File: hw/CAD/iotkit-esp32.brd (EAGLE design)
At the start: 87.3 x 72.4 mm, 14 parts, among them IC1 MCP23017SP 0x20

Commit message: Stepper an 5V
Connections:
- removed net +5V: (+)STEPPER1.1, (+)STEPPER2.1, (+)STEPPER3.1, STEPPER1.10, STEPPER2.10
- net 5V: now also (+)STEPPER1.1, (+)STEPPER2.1, (+)STEPPER3.1, STEPPER1.10, STEPPER2.10
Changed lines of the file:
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@@
 <contactref element="U$2" pad="19"/>
 <contactref element="U$1" pad="5V"/>
+<contactref element="STEPPER2" pad="10"/>
+<contactref element="(+)STEPPER3" pad="1"/>
+<contactref element="STEPPER1" pad="10"/>
+<contactref element="(+)STEPPER2" pad="1"/>
+<contactref element="(+)STEPPER1" pad="1"/>
+<wire x1="35.56" y1="68.58" x2="50.8" y2="68.58" width="0" layer="19" extent="1-1"/>
+<wire x1="20.32" y1="68.58" x2="35.56" y2="68.58" width="0" layer="19" extent="1-1"/>
+<wire x1="49.53" y1="38.1" x2="50.8" y2="68.58" width="0" layer="19" extent="1-1"/>
+<wire x1="35.56" y1="30.48" x2="49.53" y2="38.1" width="0" layer="19" extent="1-1"/>
+<wire x1="76.2" y1="38.1" x2="49.53" y2="38.1" width="0" layer="19" extent="1-1"/>
 <wire x1="5.09" y1="5.09" x2="35.56" y2="30.48" width="0" layer="19" extent="1-1"/>
 </signal>
@@
 <wire x1="5.09" y1="27.95" x2="6.91" y2="64.77" width="0" layer="19" extent="1-1"/>
 </signal>
-<signal name="+5V">
-<contactref element="STEPPER1" pad="10"/>
-<contactref element="(+)STEPPER2" pad="1"/>
-<contactref element="(+)STEPPER1" pad="1"/>
-<contactref element="STEPPER2" pad="10"/>
-<contactref element="(+)STEPPER3" pad="1"/>
-<wire x1="49.53" y1="38.1" x2="76.2" y2="38.1" width="0" layer="19" extent="1-1"/>
-<wire x1="35.56" y1="68.58" x2="49.53" y2="38.1" width="0" layer="19" extent="1-1"/>
-<wire x1="20.32" y1="68.58" x2="35.56" y2="68.58" width="0" layer="19" extent="1-1"/>
-<wire x1="50.8" y1="68.58" x2="49.53" y2="38.1" width="0" layer="19" extent="1-1"/>
-</signal>
 <signal name="PA0">

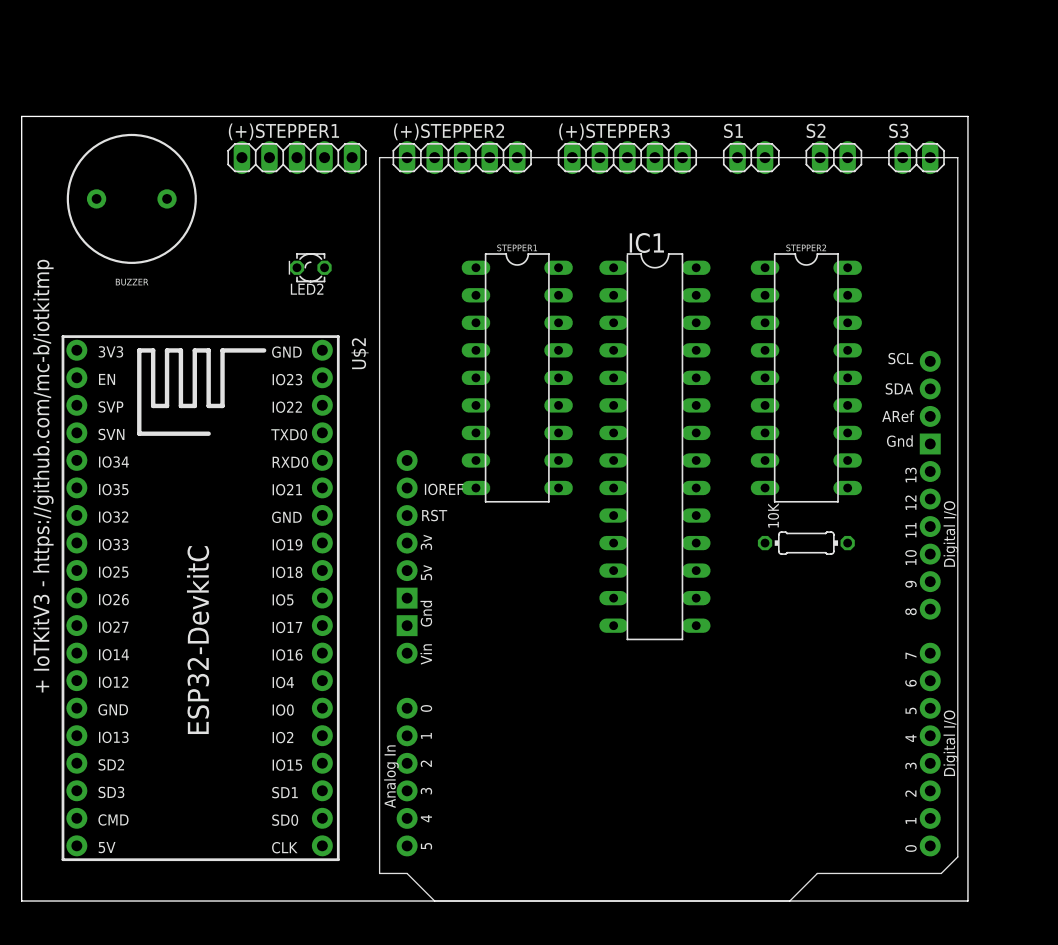
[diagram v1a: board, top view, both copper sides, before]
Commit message: Breite ESP32 falsch
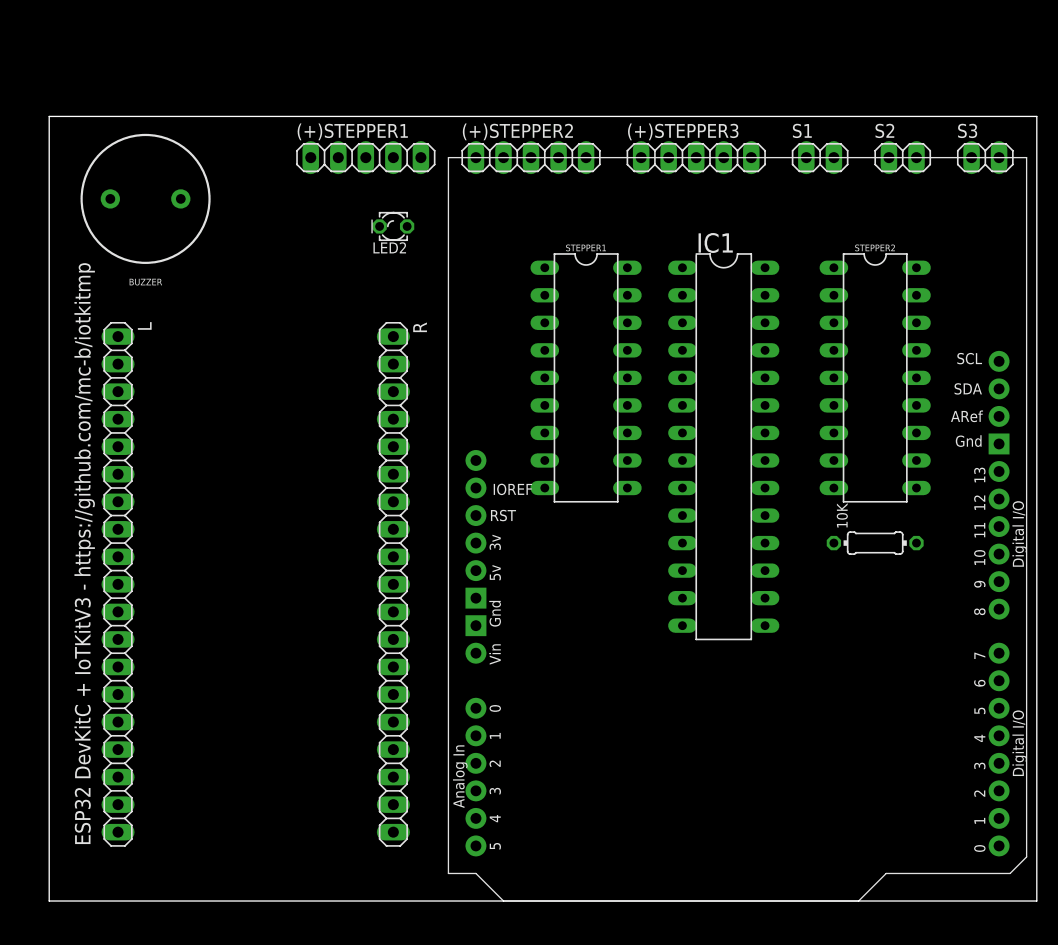
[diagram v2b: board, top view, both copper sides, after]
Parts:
- removed U$2: ESP32DEVKITC, relswitch:ESP32-DEVKITC
- added L, R: (no value), pinhead:1X19
- moved LED2 8.52 mm to (34.3, 62.2)
- moved S3 6.35 mm to (88.9, 68.6)
- moved U$1 6.35 mm to (66.0, 34.3)
- moved (+)STEPPER1 6.35 mm to (31.8, 68.6)
- moved (+)STEPPER2 6.35 mm to (47.0, 68.6)
- moved STEPPER1 6.35 mm to (52.1, 48.3)
- moved (+)STEPPER3 6.35 mm to (62.2, 68.6)
- moved 10K 6.35 mm to (78.7, 33.0)
- moved IC1 6.35 mm to (64.8, 41.9)
- moved S1 6.35 mm to (73.7, 68.6)
- moved S2 6.35 mm to (81.3, 68.6)
- moved STEPPER2 6.35 mm to (78.7, 48.3)
- moved BUZZER 1.27 mm to (11.4, 64.8)
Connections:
- net 3V3: now also L.1; no longer U$2.1
- net 5V: now also L.19; no longer U$2.19
- net A2: now also L.7; no longer U$2.7
- net A3: now also L.8; no longer U$2.8
- net A4: now also L.5; no longer U$2.5
- net A5: now also L.6; no longer U$2.6
- net BUZ: now also L.10; no longer U$2.10
- net D0: now also R.5; no longer U$2.34
- net D1: now also R.4; no longer U$2.35
- net D10: now also L.11; no longer U$2.11
- net D11: now also R.6; no longer U$2.33
- net D12: now also R.3; no longer U$2.36
- net D13: now also R.2; no longer U$2.37
- net D2: now also L.13; no longer U$2.13
- net D3: now also L.15; no longer U$2.15
- net D4: now also L.12; no longer U$2.12
- net D5: now also R.16; no longer U$2.23
- net D6: now also R.12; no longer U$2.27
- net D7: now also R.11; no longer U$2.28
- net D8: now also R.9; no longer U$2.30
- net D9: now also R.8; no longer U$2.31
- net GND: now also L.14, R.1, R.7; no longer U$2.14, U$2.32, U$2.38
- net LED1: now also R.10; no longer U$2.29
- net SCL: now also R.13; no longer U$2.26
- net SDA: now also R.15; no longer U$2.24
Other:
- board size 87.3 x 72.4 mm -> 91.1 x 72.4 mm
- board text added: "ESP32 DevKitC + IoTKitV3 - https://github.com/mc-b/iotkitmp"
- board text removed: "+ IoTKitV3 - https://github.com/mc-b/iotkitmp"

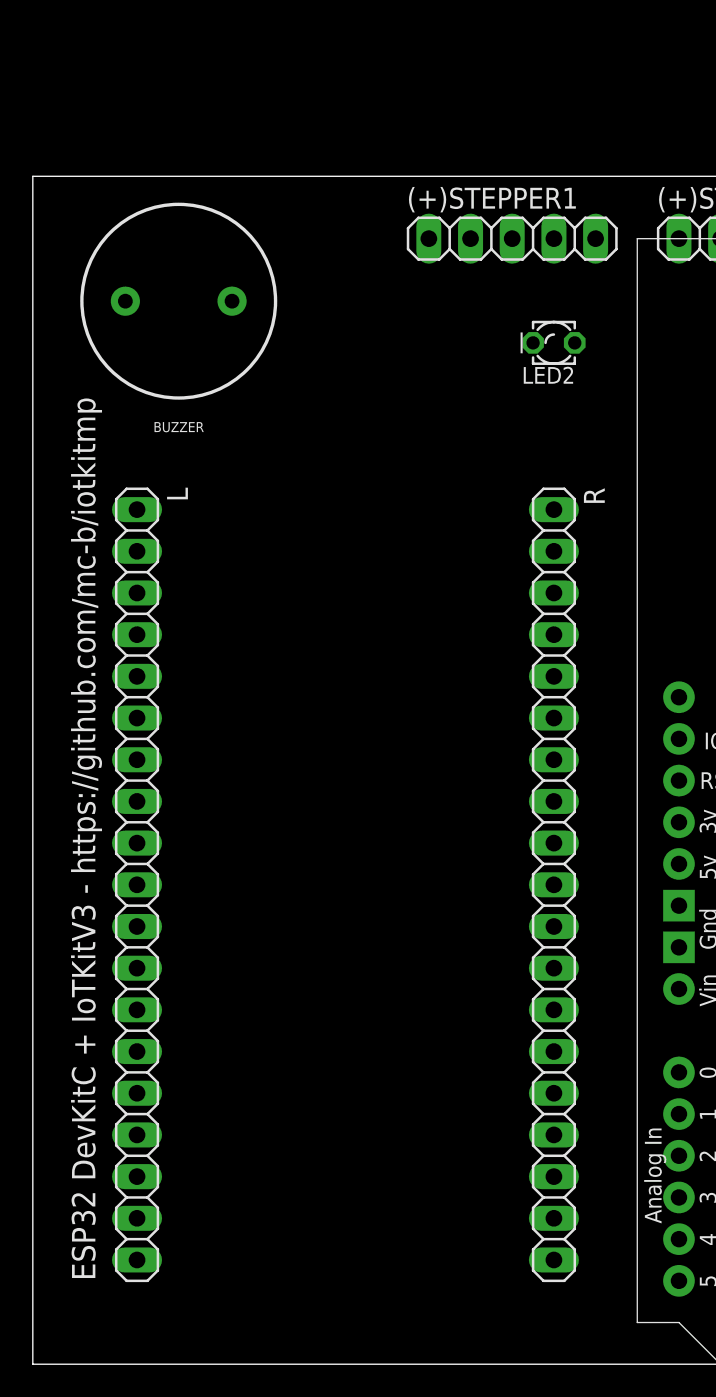
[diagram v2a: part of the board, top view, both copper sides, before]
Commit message: M5Stack Core2 Erweiterungen
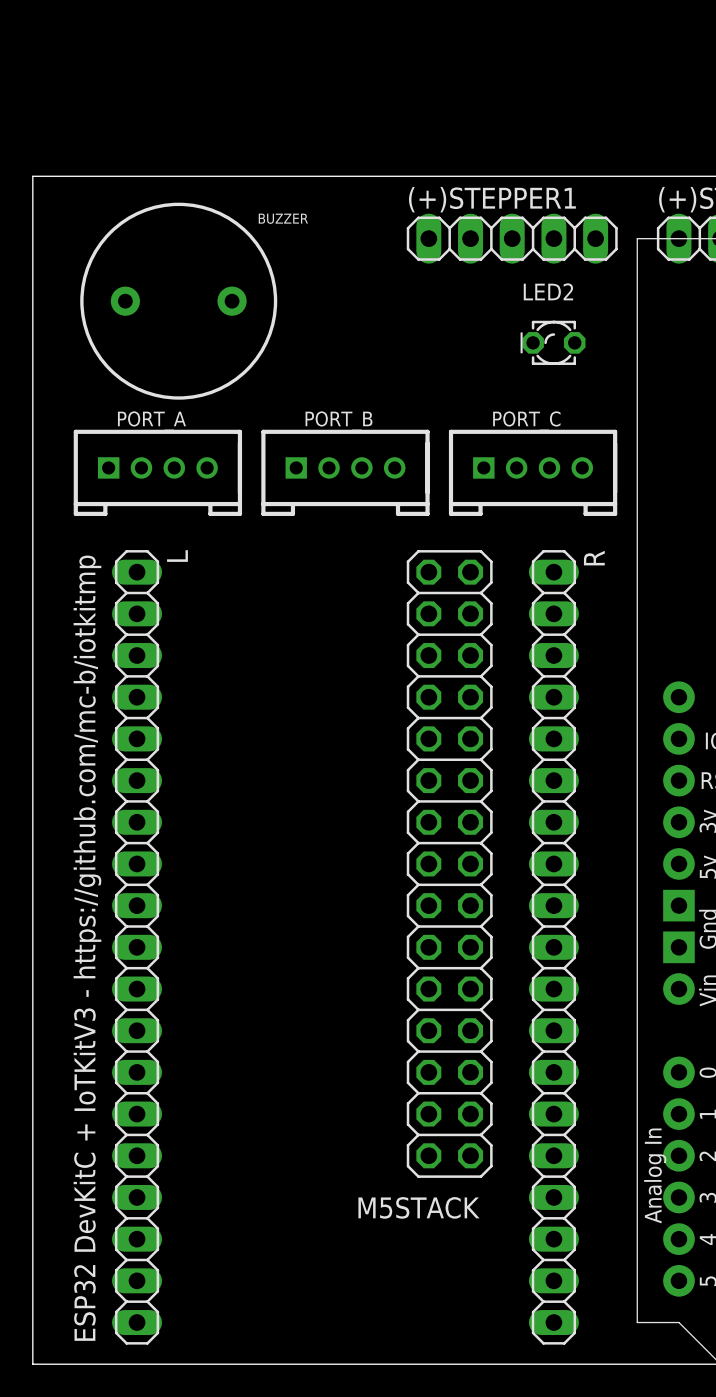
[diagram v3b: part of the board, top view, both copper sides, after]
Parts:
- added M5STACK: (no value), pinhead:2X15
- added PORT_A, PORT_B, PORT_C: I2C, Seeed-Connector:HW4-2.0
- moved L 3.81 mm to (8.89, 25.4)
- moved R 3.81 mm to (34.3, 25.4)
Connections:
- net 3V3: now also M5STACK.12
- net 5V: now also M5STACK.28, PORT_A.3, PORT_B.3, PORT_C.3
- net A2: now also M5STACK.2
- net A3: now also M5STACK.4
- net A4: now also M5STACK.14
- net A5: now also M5STACK.13
- net D0: now also M5STACK.15, PORT_C.1
- net D1: now also M5STACK.16, PORT_C.2
- net D10: now also M5STACK.8
- net D11: now also M5STACK.7
- net D12: now also M5STACK.9
- net D13: now also M5STACK.11
- net D2: now also M5STACK.23
- net D3: now also M5STACK.22
- net D4: now also M5STACK.24
- net D8: now also M5STACK.10, PORT_B.2
- net D9: now also M5STACK.21, PORT_B.1
- net GND: now also M5STACK.1, M5STACK.3, M5STACK.5, PORT_A.4, PORT_B.4, PORT_C.4
- net SCL: now also M5STACK.20, PORT_A.1
- net SDA: now also M5STACK.19, PORT_A.2

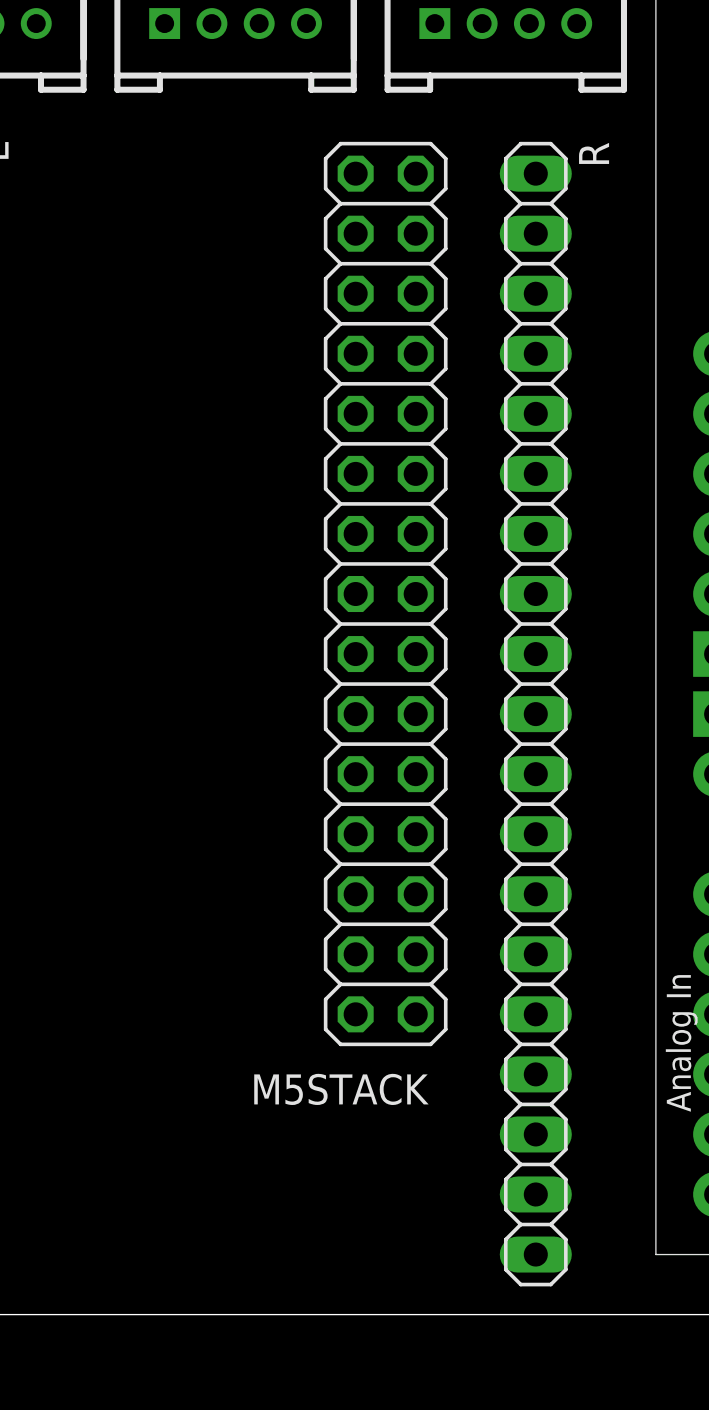
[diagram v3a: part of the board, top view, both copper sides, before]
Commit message: M5stack Seitenverkehrt korr.
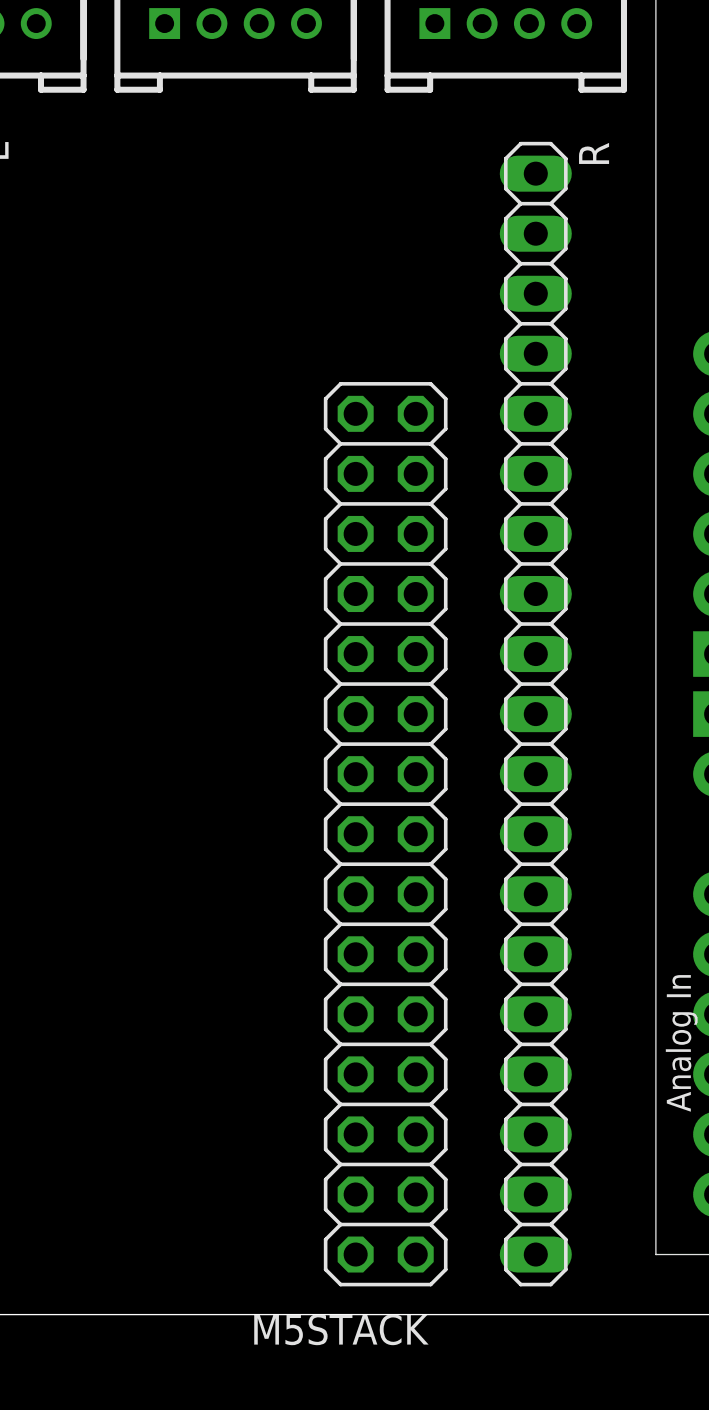
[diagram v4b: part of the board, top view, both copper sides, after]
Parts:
- moved M5STACK 10.2 mm to (27.9, 20.3)
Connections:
- net 3V3: now also M5STACK.11; no longer M5STACK.12
- net 5V: now also M5STACK.27; no longer M5STACK.28
- net A2: now also M5STACK.1; no longer M5STACK.2
- net A3: now also M5STACK.3; no longer M5STACK.4
- net A4: now also M5STACK.13; no longer M5STACK.14
- net A5: now also M5STACK.14; no longer M5STACK.13
- net D0: now also M5STACK.16; no longer M5STACK.15
- net D1: now also M5STACK.15; no longer M5STACK.16
- net D10: now also M5STACK.7; no longer M5STACK.8
- net D11: now also M5STACK.8; no longer M5STACK.7
- net D12: now also M5STACK.10; no longer M5STACK.9
- net D13: now also M5STACK.12; no longer M5STACK.11
- net D2: now also M5STACK.24; no longer M5STACK.23
- net D3: now also M5STACK.21; no longer M5STACK.22
- net D4: now also M5STACK.23; no longer M5STACK.24
- net D8: now also M5STACK.9; no longer M5STACK.10
- net D9: now also M5STACK.22; no longer M5STACK.21
- net GND: now also M5STACK.2, M5STACK.4, M5STACK.6; no longer M5STACK.1, M5STACK.3, M5STACK.5
- net SCL: now also M5STACK.19; no longer M5STACK.20
- net SDA: now also M5STACK.20; no longer M5STACK.19
